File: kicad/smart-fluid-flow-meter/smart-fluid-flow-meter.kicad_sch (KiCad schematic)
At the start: 2 parts, among them U1 ESP32-WROOM-32

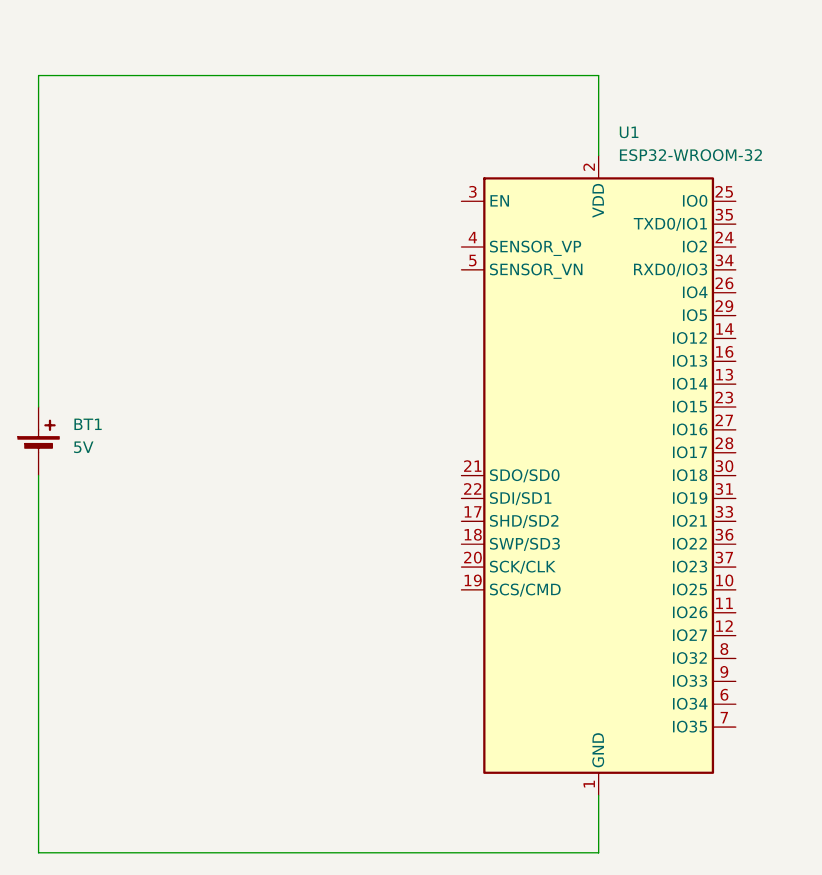
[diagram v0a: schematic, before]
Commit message: Add power LED and yf-s201 to kicad schematic
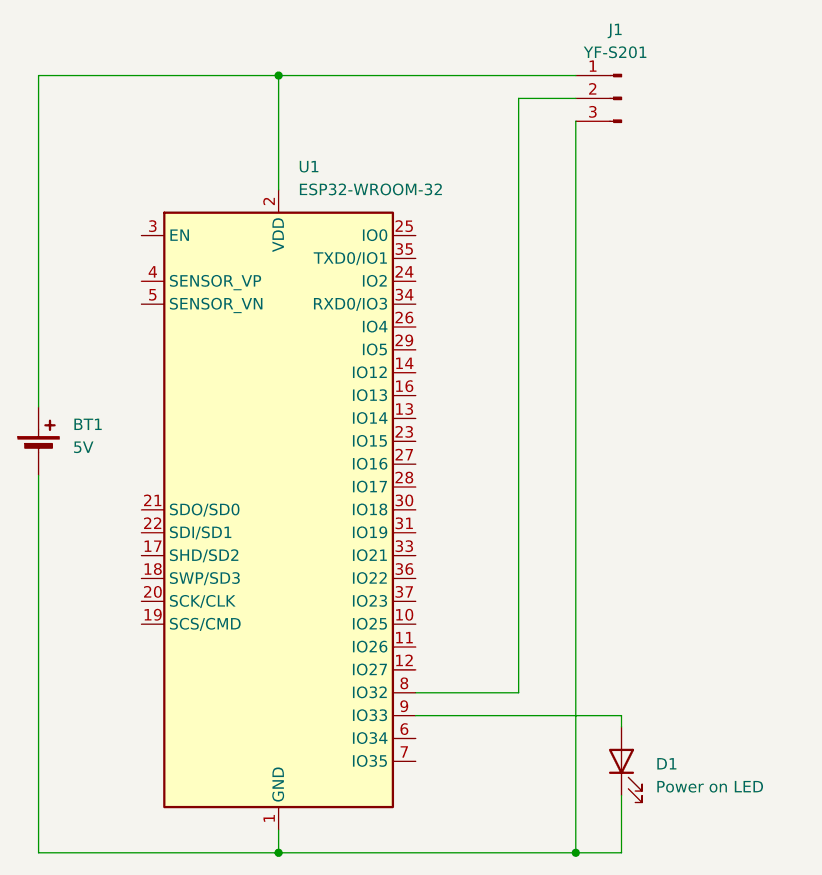
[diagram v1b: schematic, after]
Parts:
- added D1: Power on LED, symbol Device:LED
- added J1: YF-S201, symbol Connector:Conn_01x03_Pin
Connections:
- net at BT1.2 (-), U1.1 (GND), U1.15 (GND)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: now also D1.1 (K), J1.3 (Pin_3)
- net at BT1.1 (+), U1.2 (VDD): now also J1.1 (Pin_1)
- net at U1.8 (IO32): now also J1.2 (Pin_2)
- net at U1.9 (IO33): now also D1.2 (A)
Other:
- moved on the sheet: U1

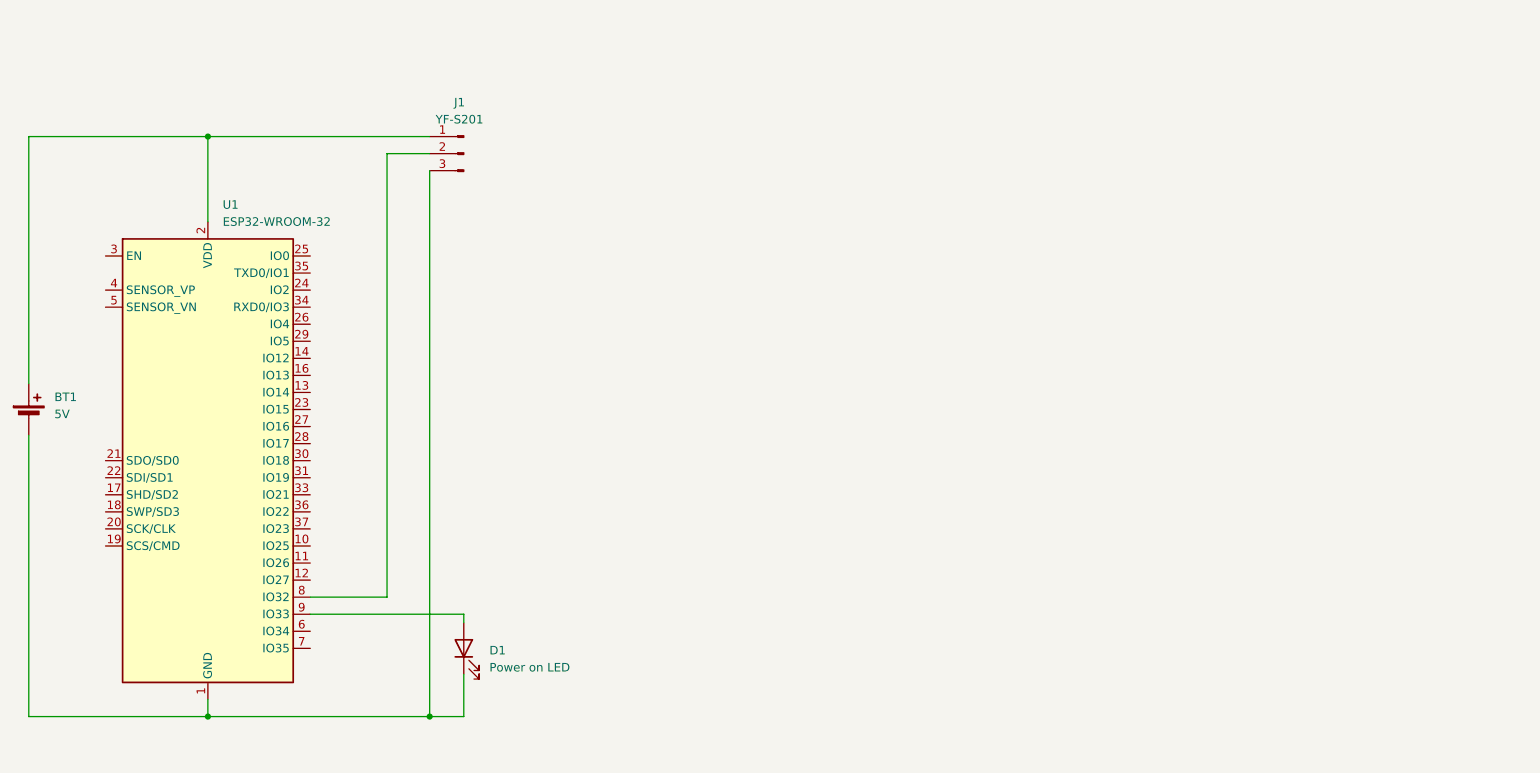
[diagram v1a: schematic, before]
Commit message: Add resistors to water flow meter in schematic. Add notes to schematic
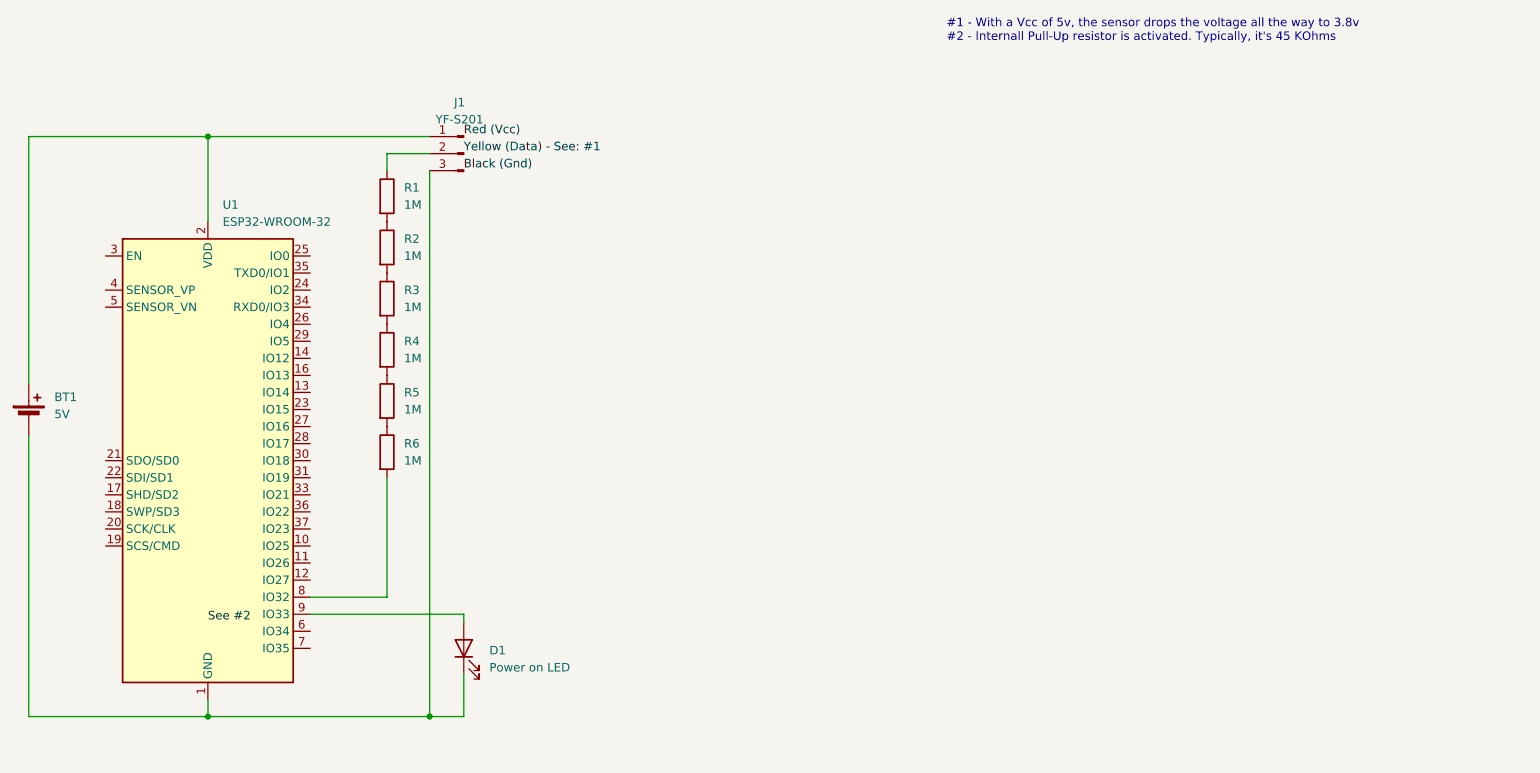
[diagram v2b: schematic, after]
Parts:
- added R1, R2, R3, R4, R5, R6: 1M, symbol Device:R
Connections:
- net at U1.8 (IO32): now also R6.2; no longer J1.2 (Pin_2)
- new net: R4.2, R5.1
- new net: R5.2, R6.1
- new net: J1.2 (Pin_2), R1.1
- new net: R1.2, R2.1
- new net: R3.2, R4.1
- new net: R2.2, R3.1
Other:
- note added: "#1 - With a Vcc of 5v, the sensor drops the voltage all the way to 3.8v #2 - Internall Pull-Up resistor is activated. Typically, it's 45 KOhms"

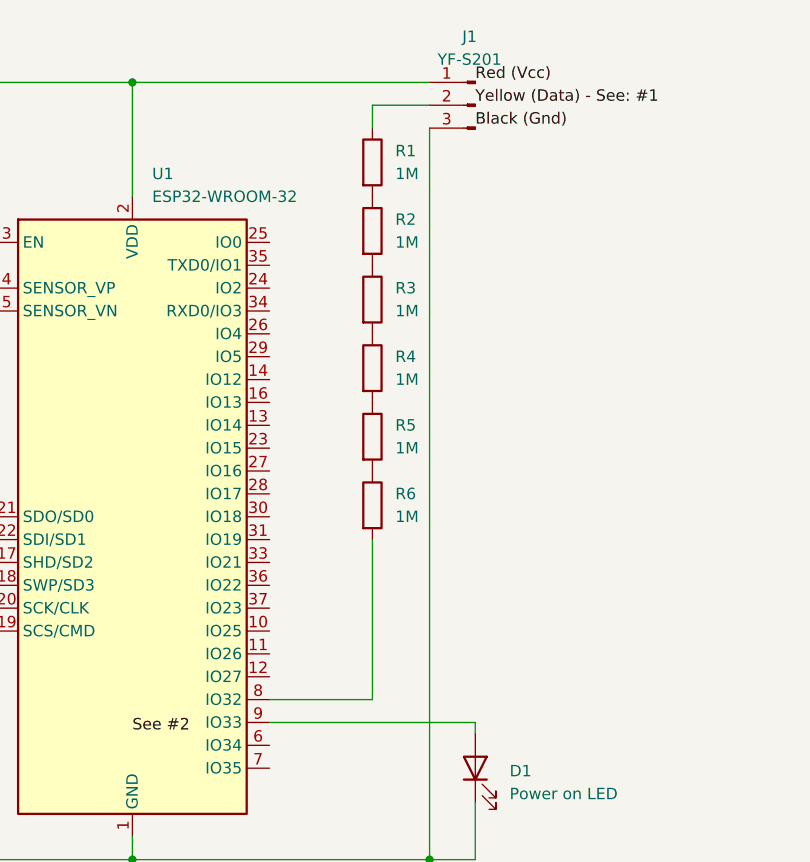
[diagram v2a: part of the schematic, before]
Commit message: Replace 6 1MOhm resistors with 2 3.3MOhm resistors in schematic (#55)
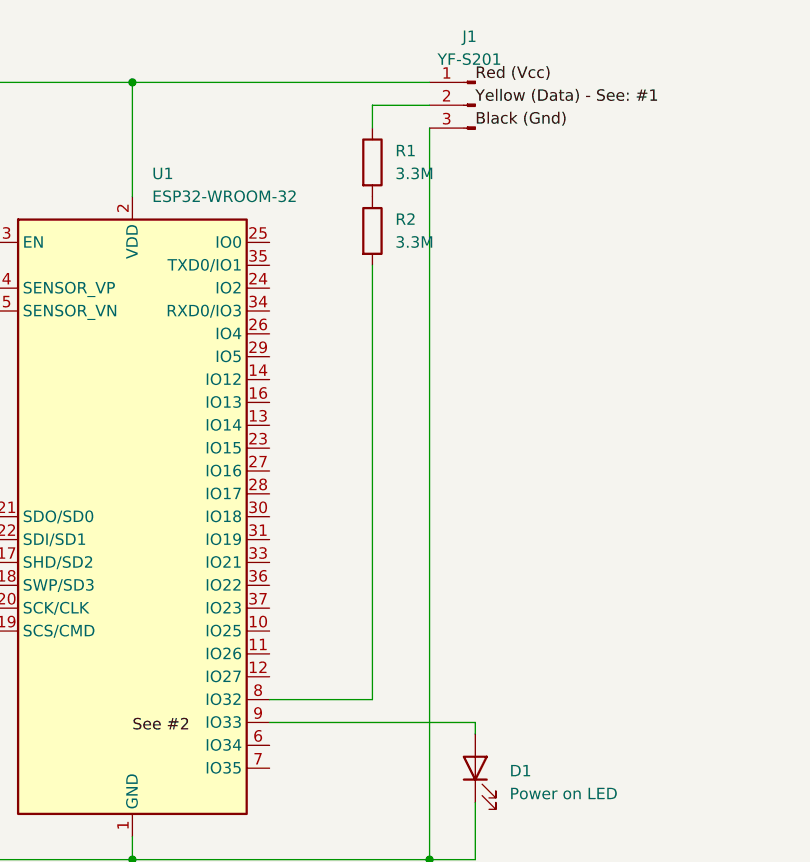
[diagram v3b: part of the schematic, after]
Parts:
- removed R3, R4, R5, R6: 1M, symbol Device:R
- R1, R2: value 1M -> 3.3M
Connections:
- net at U1.8 (IO32): now also R2.2

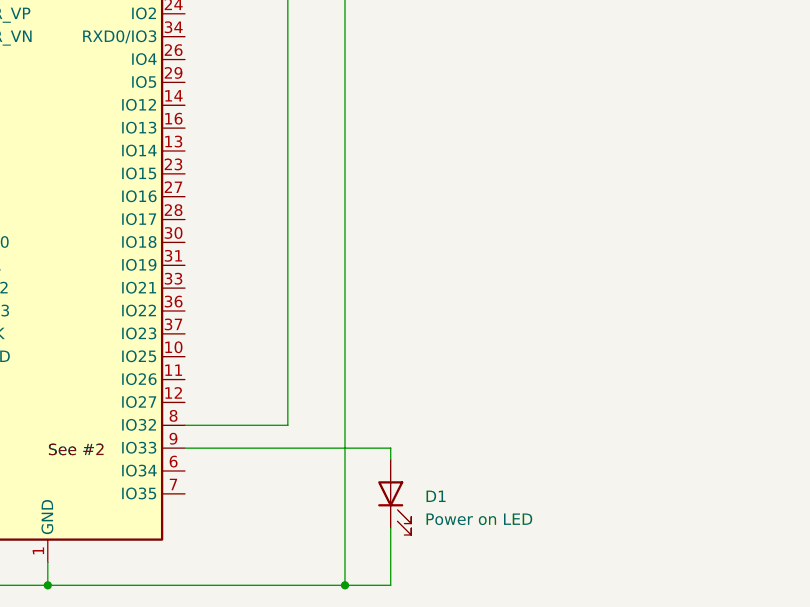
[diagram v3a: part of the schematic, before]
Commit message: Add factory reset button (#56)
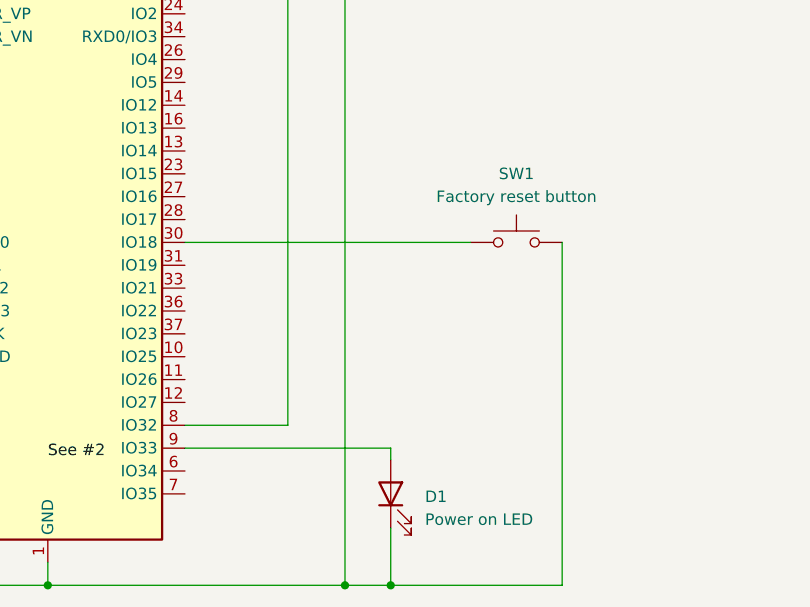
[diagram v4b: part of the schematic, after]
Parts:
- added SW1: Factory reset button, symbol Switch:SW_Push
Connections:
- net at BT1.2 (-), D1.1 (K), J1.3 (Pin_3)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: now also SW1.2
- net at U1.30 (IO18): now also SW1.1
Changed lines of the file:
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@@
 		(color 0 0 0 0)
 	)
+	(junction
+		(at 138.43 120.65)
+		(diameter 0)
+		(color 0 0 0 0)
+	)
 	(wire
 		(pts
@@
 	(wire
 		(pts
+			(xy 157.48 82.55) (xy 157.48 120.65)
+		)
+		(stroke
+			(width 0)
+			(type default)
+		)
+	)
+	(wire
+		(pts
 			(xy 73.66 34.29) (xy 100.33 34.29)
 		)
@@
 	(wire
 		(pts
+			(xy 147.32 82.55) (xy 115.57 82.55)
+		)
+		(stroke
+			(width 0)
+			(type default)
+		)
+	)
+	(wire
+		(pts
 			(xy 73.66 120.65) (xy 100.33 120.65)
 		)
@@
 		(pts
 			(xy 115.57 102.87) (xy 127 102.87)
+		)
+		(stroke
+			(width 0)
+			(type default)
+		)
+	)
+	(wire
+		(pts
+			(xy 138.43 120.65) (xy 157.48 120.65)
 		)
 		(stroke
@@
 					(unit 1)
 				)
+			)
+		)
+	)
+	(symbol
+		(lib_id "Switch:SW_Push")
+		(at 152.4 82.55 0)
+		(unit 1)
+		(exclude_from_sim no)
+		(in_bom yes)
+		(on_board yes)
+		(dnp no)
+		(fields_autoplaced yes)
+		(property "Reference" "SW1"
+			(at 152.4 74.93 0)
+			(effects
+				(font
+					(size 1.27 1.27)
+				)
+			)
+		)
+		(property "Value" "Factory reset button"
+			(at 152.4 77.47 0)
+			(effects
+				(font
+					(size 1.27 1.27)
+				)
+			)
+		)
+		(property "Footprint" ""
+			(at 152.4 77.47 0)
+			(effects
+				(font
+					(size 1.27 1.27)
+				)
+				(hide yes)
+			)
+		)
+		(property "Datasheet" "~"
+			(at 152.4 77.47 0)
+			(effects
+				(font
+					(size 1.27 1.27)
+				)
+				(hide yes)
+			)
+		)
+		(property "Description" "Push button switch, generic, two pins"
+			(at 152.4 82.55 0)
+			(effects
+				(font
+					(size 1.27 1.27)
+				)
+				(hide yes)
+			)
+		)
+		(pin "2"
+		)
+		(pin "1"
+		)
+		(instances
+			(project ""
+				(path "/39fefc38-68db-426d-adc7-52db70b33c24"
+					(reference "SW1")
+					(unit 1)
+				)
